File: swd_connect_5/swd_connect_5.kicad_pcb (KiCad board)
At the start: 2 copper layers, 49 x 18 mm, 2 parts, among them J2 Link-E Receptacle, J3 swd-connect-5

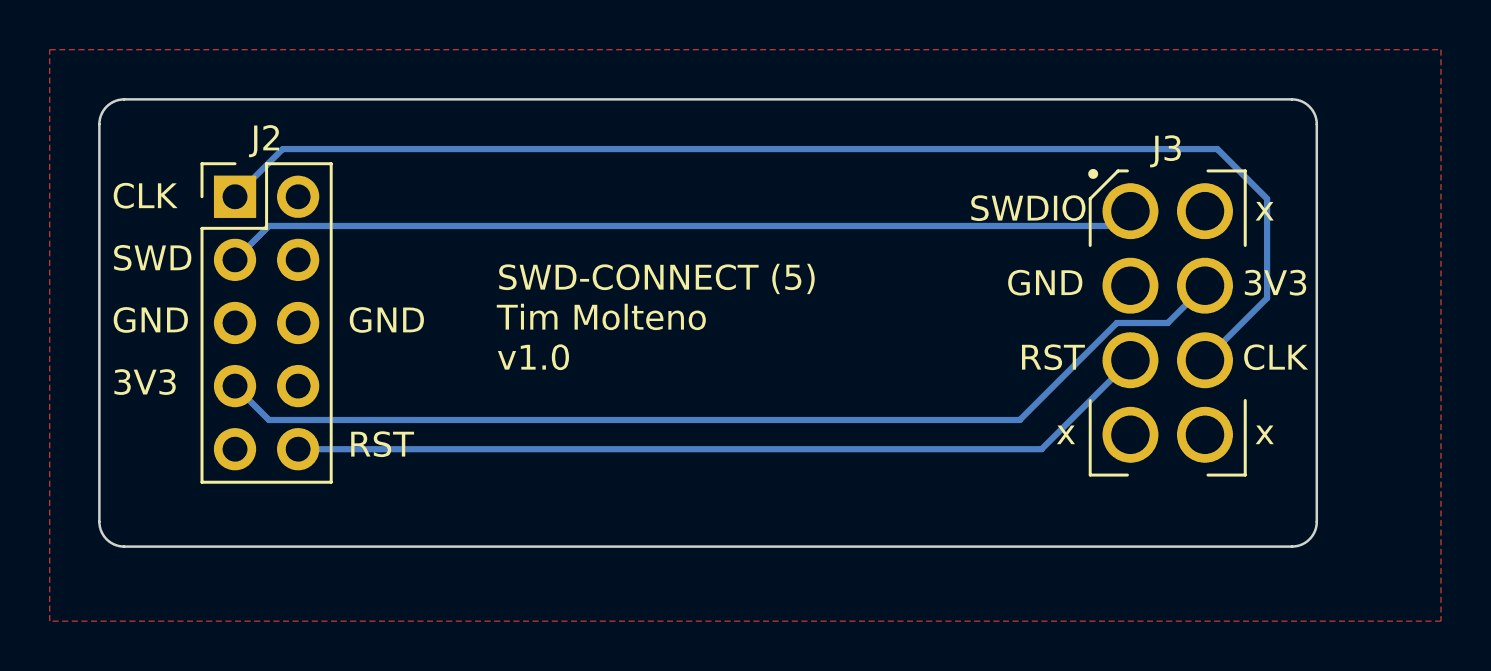
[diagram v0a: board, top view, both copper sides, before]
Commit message: Update footprints to include silkscreen pin identifiers
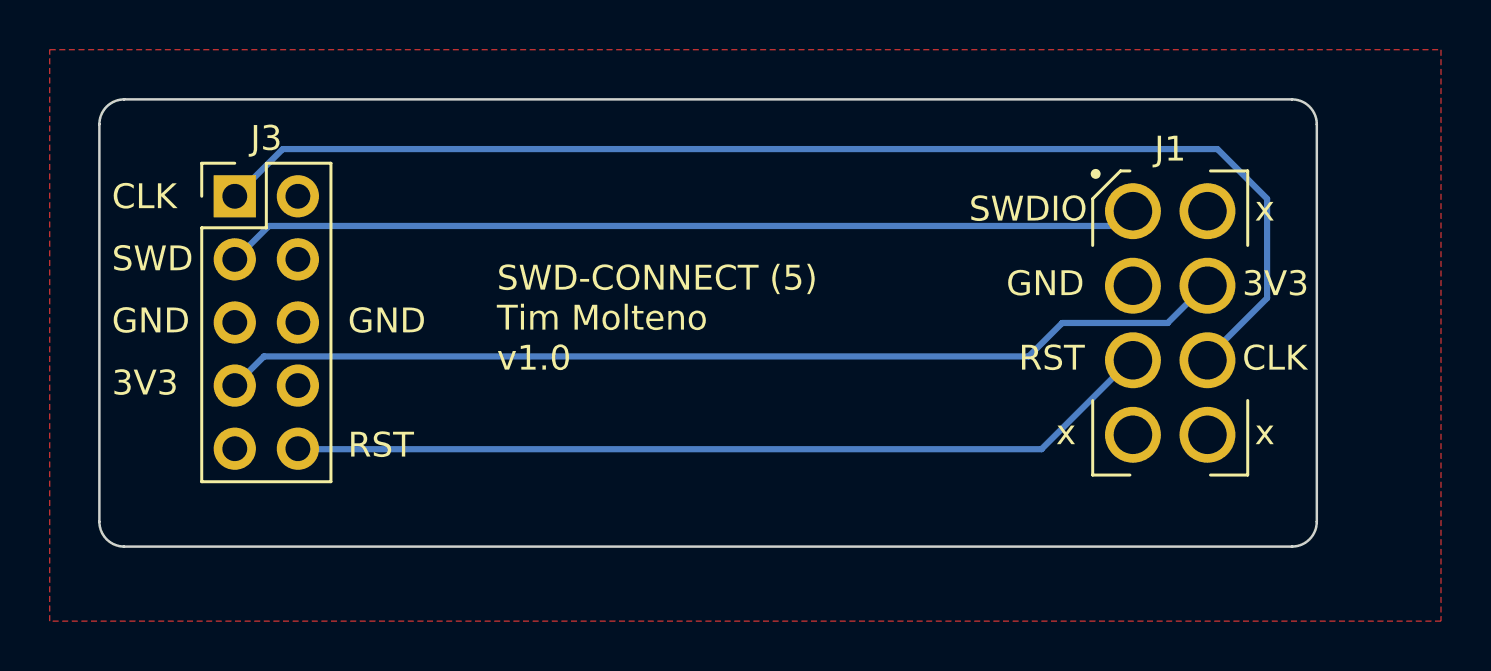
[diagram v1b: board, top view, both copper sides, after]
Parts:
- removed J2: Link-E Receptacle, Connector_PinHeader_2.54mm:PinHeader_2x05_P2.54mm_Vertical
- added J1: swd-connect-5, swd-connect:swd-connect-5-programmer, F.Cu at (159.1, 70.0)
- J3: value swd-connect-5 -> Link-E Receptacle; footprint ZL4AA:swd-connect-5-programmer -> Connector_PinHeader_2.54mm:PinHeader_2x05_P2.54mm_Vertical
- moved J3 37.9 mm to (121.5, 64.9)
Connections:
- J3 pad 2: GND -> unconnected-(J3-RX-Pad2)
- J3 pad 4: Net-(J2-RST) -> unconnected-(J3-TX-Pad4)
- J3 pad 5: Net-(J2-SWCLK) -> GND
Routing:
- net Net-(J2-SWCLK): track 50.7 -> 0.00 mm
- net Net-(J1-3V3): track 0.00 -> 40.7 mm
- net Net-(J2-RST): track 35.0 -> 0.00 mm
- net Net-(J1-RST): track 0.00 -> 35.0 mm
- net Net-(J1-SWCLK): track 36.9 -> 50.7 mm
- net Net-(J1-SWD): track 41.8 -> 36.9 mm
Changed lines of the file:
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@@
   )
   (net 0 "")
-  (net 1 "Net-(J2-SWCLK)")
-  (net 2 "unconnected-(J2-RX-Pad2)")
-  (net 3 "Net-(J2-SWDIO)")
-  (net 4 "unconnected-(J2-TX-Pad4)")
+  (net 1 "Net-(J1-SWD)")
+  (net 2 "Net-(J1-3V3)")
+  (net 3 "Net-(J1-RST)")
+  (net 4 "Net-(J1-SWCLK)")
   (net 5 "GND")
-  (net 6 "Net-(J3-3V3)")
-  (net 7 "unconnected-(J2-3V3-Pad8)")
-  (net 8 "unconnected-(J2-5V-Pad9)")
-  (net 9 "Net-(J2-RST)")
-  (footprint "ZL4AA:swd-connect-5-programmer" (layer "F.Cu")
-    (at 159 70)
+  (net 6 "unconnected-(J3-RX-Pad2)")
+  (net 7 "unconnected-(J3-TX-Pad4)")
+  (net 8 "unconnected-(J3-3V3-Pad8)")
+  (net 9 "unconnected-(J3-5V-Pad9)")
+  (footprint "swd-connect:swd-connect-5-programmer" (layer "F.Cu")
+    (at 159.1 70)
     (property "Sheetfile" "swd_connect_5.kicad_sch")
     (property "Sheetname" "")
@@
     (property "ki_description" "Simple SWD programming footprint (MCU side)")
     (attr smd exclude_from_bom)
-    (fp_text reference "J3" (at 0 -7) (layer "F.SilkS")
+    (fp_text reference "J1" (at 0 -7) (layer "F.SilkS")
         (effects (font (size 1 1) (thickness 0.15)))
     )
@@
     (pad "" np_thru_hole circle (at 1.5 4.5) (size 2.25 2.25) (drill 1.55) (layers "F&B.Cu" "*.Mask"))
     (pad "1" thru_hole circle (at -1.5 -4.5) (size 2.25 2.25) (drill 1.55) (layers "*.Cu" "*.Mask")
-      (net 3 "Net-(J2-SWDIO)") (pinfunction "SWD") (pintype "unspecified"))
+      (net 1 "Net-(J1-SWD)") (pinfunction "SWD") (pintype "unspecified"))
     (pad "2" thru_hole circle (at -1.5 -1.5) (size 2.25 2.25) (drill 1.55) (layers "*.Cu" "*.Mask")
       (net 5 "GND") (pinfunction "GND") (pintype "unspecified"))
     (pad "3" thru_hole circle (at 1.5 -1.5) (size 2.25 2.25) (drill 1.55) (layers "*.Cu" "*.Mask")
-      (net 6 "Net-(J3-3V3)") (pinfunction "3V3") (pintype "unspecified"))
+      (net 2 "Net-(J1-3V3)") (pinfunction "3V3") (pintype "unspecified"))
     (pad "4" thru_hole circle (at -1.5 1.5) (size 2.25 2.25) (drill 1.55) (layers "*.Cu" "*.Mask")
-      (net 9 "Net-(J2-RST)") (pinfunction "RST") (pintype "unspecified"))
+      (net 3 "Net-(J1-RST)") (pinfunction "RST") (pintype "unspecified"))
     (pad "5" thru_hole circle (at 1.5 1.5) (size 2.25 2.25) (drill 1.55) (layers "*.Cu" "*.Mask")
-      (net 1 "Net-(J2-SWCLK)") (pinfunction "SWCLK") (pintype "unspecified"))
+      (net 4 "Net-(J1-SWCLK)") (pinfunction "SWCLK") (pintype "unspecified"))
   )
   (footprint "Connector_PinHeader_2.54mm:PinHeader_2x05_P2.54mm_Vertical" (layer "F.Cu")
-    (at 121.46 64.92)
+    (at 121.45 64.9)
     (descr "Through hole straight pin header, 2x05, 2.54mm pitch, double rows")
     (tags "Through hole pin header THT 2x05 2.54mm double row")
@@
     (property "Sim.Enable" "0")
     (property "ki_description" "Link_E  connector for programming WCH chips including ch32v series using SWD.")
-    (attr through_hole exclude_from_bom)
-    (fp_text reference "J2" (at 1.27 -2.33) (layer "F.SilkS")
+    (attr through_hole)
+    (fp_text reference "J3" (at 1.27 -2.33) (layer "F.SilkS")
         (effects (font (size 1 1) (thickness 0.15)))
     )
@@
       (stroke (width 0.1) (type solid)) (layer "F.Fab"))
     (pad "1" thru_hole rect (at 0 0) (size 1.7 1.7) (drill 1) (layers "*.Cu" "*.Mask")
-      (net 1 "Net-(J2-SWCLK)") (pinfunction "SWCLK") (pintype "unspecified"))
+      (net 4 "Net-(J1-SWCLK)") (pinfunction "SWCLK") (pintype "unspecified"))
     (pad "2" thru_hole oval (at 2.54 0) (size 1.7 1.7) (drill 1) (layers "*.Cu" "*.Mask")
-      (net 2 "unconnected-(J2-RX-Pad2)") (pinfunction "RX") (pintype "unspecified"))
+      (net 6 "unconnected-(J3-RX-Pad2)") (pinfunction "RX") (pintype "unspecified"))
     (pad "3" thru_hole oval (at 0 2.54) (size 1.7 1.7) (drill 1) (layers "*.Cu" "*.Mask")
-      (net 3 "Net-(J2-SWDIO)") (pinfunction "SWDIO") (pintype "unspecified"))
+      (net 1 "Net-(J1-SWD)") (pinfunction "SWDIO") (pintype "unspecified"))
     (pad "4" thru_hole oval (at 2.54 2.54) (size 1.7 1.7) (drill 1) (layers "*.Cu" "*.Mask")
-      (net 4 "unconnected-(J2-TX-Pad4)") (pinfunction "TX") (pintype "unspecified"))
+      (net 7 "unconnected-(J3-TX-Pad4)") (pinfunction "TX") (pintype "unspecified"))
     (pad "5" thru_hole oval (at 0 5.08) (size 1.7 1.7) (drill 1) (layers "*.Cu" "*.Mask")
       (net 5 "GND") (pinfunction "GND") (pintype "unspecified"))
@@
       (net 5 "GND") (pinfunction "GND") (pintype "unspecified"))
     (pad "7" thru_hole oval (at 0 7.62) (size 1.7 1.7) (drill 1) (layers "*.Cu" "*.Mask")
-      (net 6 "Net-(J3-3V3)") (pinfunction "3V3") (pintype "unspecified"))
+      (net 2 "Net-(J1-3V3)") (pinfunction "3V3") (pintype "unspecified"))
     (pad "8" thru_hole oval (at 2.54 7.62) (size 1.7 1.7) (drill 1) (layers "*.Cu" "*.Mask")
-      (net 7 "unconnected-(J2-3V3-Pad8)") (pinfunction "3V3") (pintype "unspecified"))
+      (net 8 "unconnected-(J3-3V3-Pad8)") (pinfunction "3V3") (pintype "unspecified"))
     (pad "9" thru_hole oval (at 0 10.16) (size 1.7 1.7) (drill 1) (layers "*.Cu" "*.Mask")
-      (net 8 "unconnected-(J2-5V-Pad9)") (pinfunction "5V") (pintype "unspecified"))
+      (net 9 "unconnected-(J3-5V-Pad9)") (pinfunction "5V") (pintype "unspecified"))
     (pad "10" thru_hole oval (at 2.54 10.16) (size 1.7 1.7) (drill 1) (layers "*.Cu" "*.Mask")
-      (net 9 "Net-(J2-RST)") (pinfunction "RST") (pintype "unspecified"))
+      (net 3 "Net-(J1-RST)") (pinfunction "RST") (pintype "unspecified"))
     (model "${KICAD6_3DMODEL_DIR}/Connector_PinHeader_2.54mm.3dshapes/PinHeader_2x05_P2.54mm_Vertical.wrl"
       (offset (xyz 0 0 0))
@@
     (effects (font (size 1 1) (thickness 0.15)) (justify left bottom))
   )
-  (segment (start 163 65) (end 163 69) (width 0.25) (layer "B.Cu") (net 1))
-  (segment (start 121.46 64.92) (end 123.38 63) (width 0.25) (layer "B.Cu") (net 1))
-  (segment (start 161 63) (end 163 65) (width 0.25) (layer "B.Cu") (net 1))
-  (segment (start 163 69) (end 160.5 71.5) (width 0.25) (layer "B.Cu") (net 1))
-  (segment (start 123.38 63) (end 161 63) (width 0.25) (layer "B.Cu") (net 1))
-  (segment (start 122.825 66.095) (end 156.905 66.095) (width 0.25) (layer "B.Cu") (net 3))
-  (segment (start 156.905 66.095) (end 157.5 65.5) (width 0.25) (layer "B.Cu") (net 3))
-  (segment (start 121.46 67.46) (end 122.825 66.095) (width 0.25) (layer "B.Cu") (net 3))
-  (segment (start 153.04439 73.905) (end 156.94939 70) (width 0.25) (layer "B.Cu") (net 6))
-  (segment (start 159 70) (end 160.5 68.5) (width 0.25) (layer "B.Cu") (net 6))
-  (segment (start 121.46 72.54) (end 122.825 73.905) (width 0.25) (layer "B.Cu") (net 6))
-  (segment (start 122.825 73.905) (end 153.04439 73.905) (width 0.25) (layer "B.Cu") (net 6))
-  (segment (start 156.94939 70) (end 159 70) (width 0.25) (layer "B.Cu") (net 6))
-  (segment (start 124 75.08) (end 153.92 75.08) (width 0.25) (layer "B.Cu") (net 9))
-  (segment (start 153.92 75.08) (end 157.5 71.5) (width 0.25) (layer "B.Cu") (net 9))
+  (segment (start 122.825 66.095) (end 156.905 66.095) (width 0.25) (layer "B.Cu") (net 1))
+  (segment (start 156.905 66.095) (end 157.5 65.5) (width 0.25) (layer "B.Cu") (net 1))
+  (segment (start 121.46 67.46) (end 122.825 66.095) (width 0.25) (layer "B.Cu") (net 1))
+  (segment (start 154.75 70) (end 159 70) (width 0.25) (layer "B.Cu") (net 2))
+  (segment (start 153.405 71.345) (end 154.75 70) (width 0.25) (layer "B.Cu") (net 2))
+  (segment (start 121.45 72.52) (end 122.625 71.345) (width 0.25) (layer "B.Cu") (net 2))
+  (segment (start 122.625 71.345) (end 153.405 71.345) (width 0.25) (layer "B.Cu") (net 2))
+  (segment (start 159 70) (end 160.5 68.5) (width 0.25) (layer "B.Cu") (net 2))
+  (segment (start 124 75.08) (end 153.92 75.08) (width 0.25) (layer "B.Cu") (net 3))
+  (segment (start 153.92 75.08) (end 157.5 71.5) (width 0.25) (layer "B.Cu") (net 3))
+  (segment (start 163 65) (end 163 69) (width 0.25) (layer "B.Cu") (net 4))
+  (segment (start 121.46 64.92) (end 123.38 63) (width 0.25) (layer "B.Cu") (net 4))
+  (segment (start 161 63) (end 163 65) (width 0.25) (layer "B.Cu") (net 4))
+  (segment (start 163 69) (end 160.5 71.5) (width 0.25) (layer "B.Cu") (net 4))
+  (segment (start 123.38 63) (end 161 63) (width 0.25) (layer "B.Cu") (net 4))
   (zone (net 5) (net_name "GND") (layer "F.Cu") (hatch edge 0.5)
     (connect_pads (clearance 0.2))
